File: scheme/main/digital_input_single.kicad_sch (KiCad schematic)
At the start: 5 parts, among them U22 PC817

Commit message: di & do terminals
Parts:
- added D11: BAS40-04, Package_TO_SOT_SMD:SOT-23, symbol Diode:BAS40-04
- renumbered C94 to C96, R75 to R79, R74 to R80, R78 to R81, U22 to U23
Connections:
- net in-: now also D11.1
- net at C96.1, R80.1, R81.2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: now also D11.2, D11.3
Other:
- moved on the sheet: C96, R80, R81

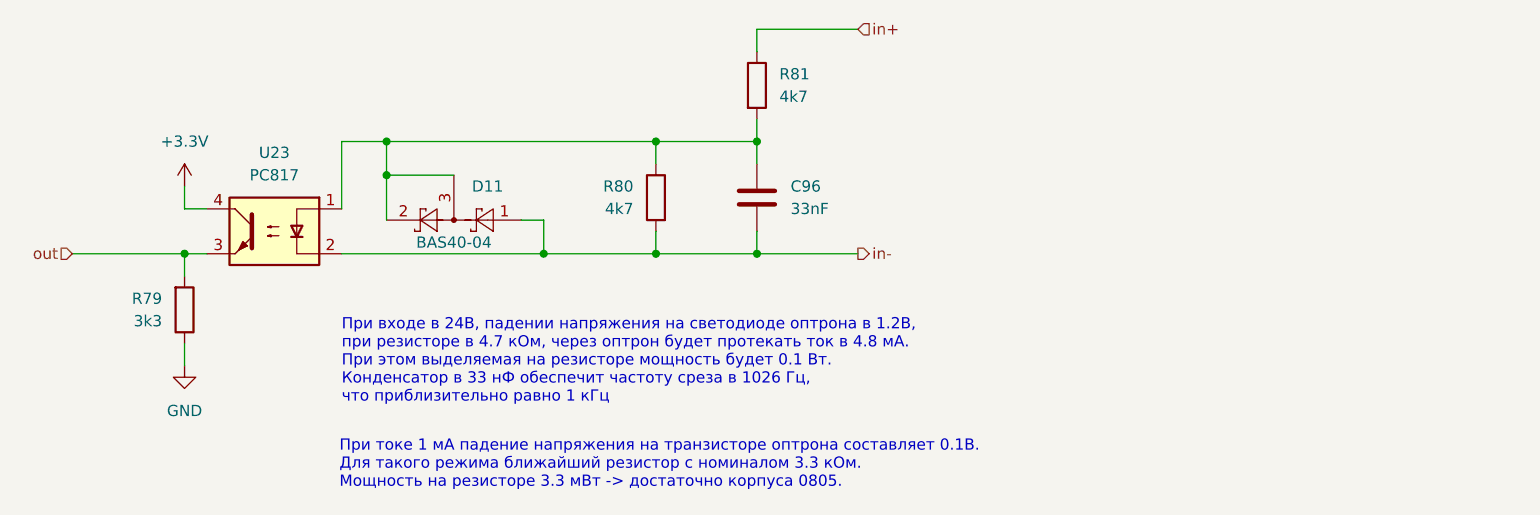
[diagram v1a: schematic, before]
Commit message: dc passive discharge schematic
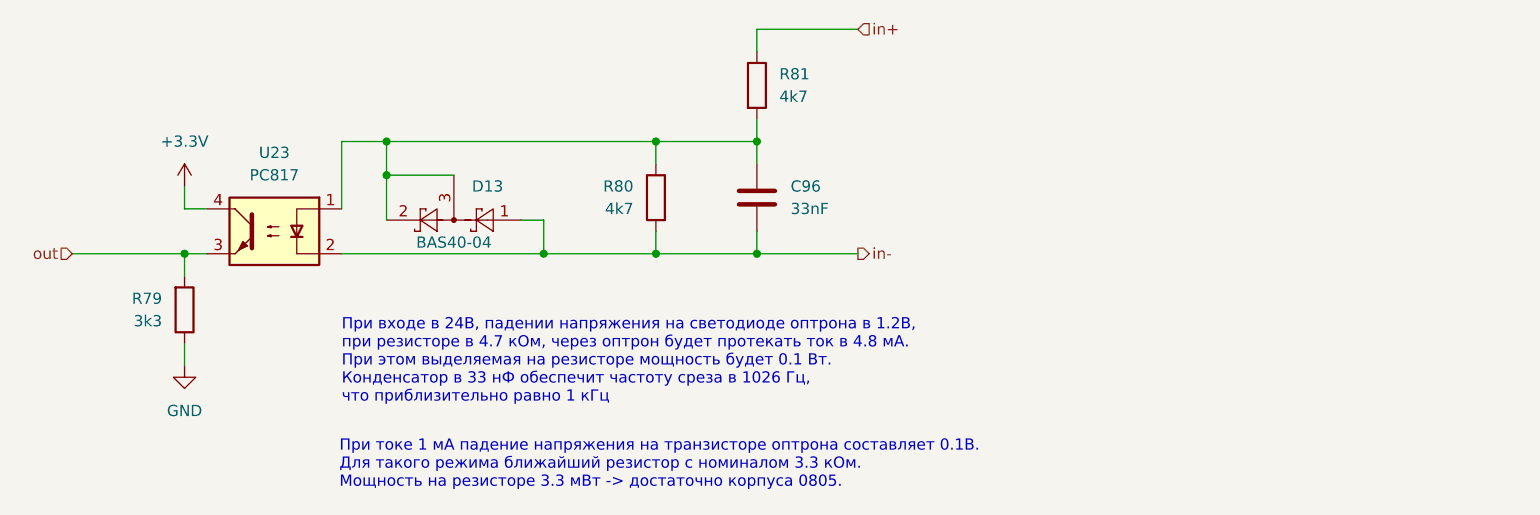
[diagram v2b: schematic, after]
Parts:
- renumbered D11 to D13
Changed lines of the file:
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@@
 		(on_board yes)
 		(dnp no)
-		(property "Reference" "D11"
+		(property "Reference" "D13"
 			(at 161.29 87.63 0)
 			(effects

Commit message: toplevel layout, can bus
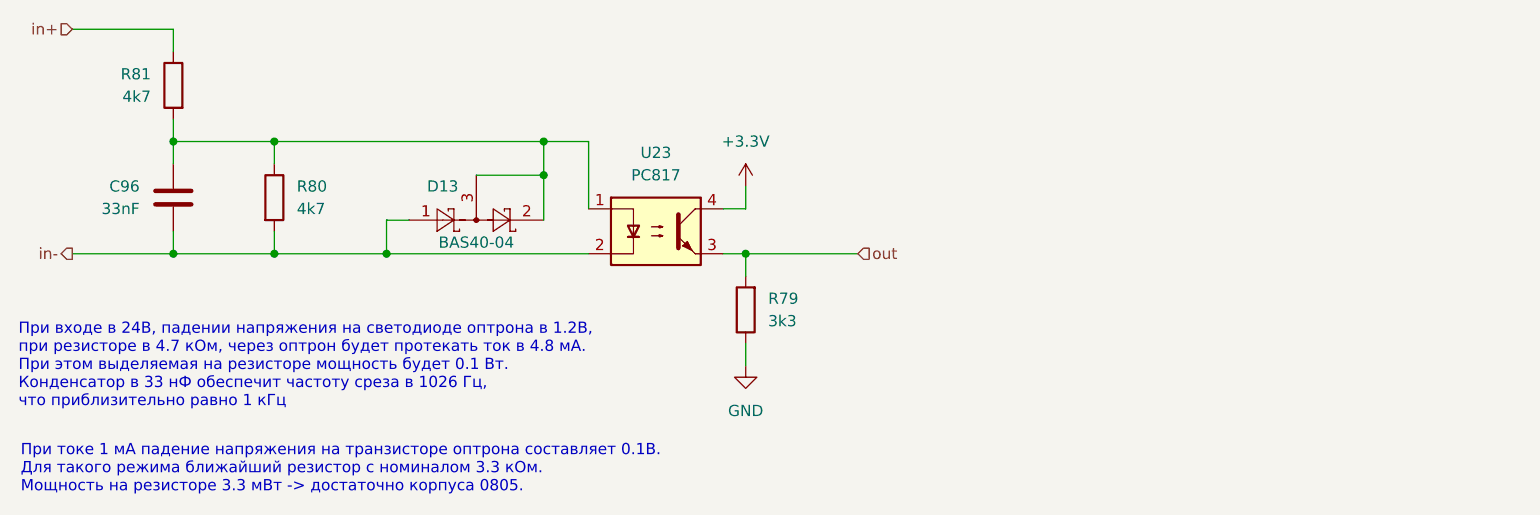
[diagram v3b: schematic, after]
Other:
- moved on the sheet: C96, D13, R79, R80, R81, U23

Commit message: boards schematic sheets & more
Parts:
- added R108: 22R, Resistor_SMD:R_0805_2012Metric, symbol Device:R
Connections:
- net out: now also R108.2; no longer R79.2, U23.3
- new net: R108.1, R79.2, U23.3
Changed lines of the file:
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@@
+	)
+	(junction
+		(at 190.5 95.25)
+		(diameter 0)
+		(color 0 0 0 0)
 	)
 	(junction
@@
 	)
 	(junction
-		(at 190.5 95.25)
-		(diameter 0)
-		(color 0 0 0 0)
-	)
-	(junction
 		(at 125.73 95.25)
 		(diameter 0)
@@
 	(wire
 		(pts
+			(xy 190.5 95.25) (xy 193.04 95.25)
+		)
+		(stroke
+			(width 0)
+			(type default)
+		)
+	)
+	(wire
+		(pts
 			(xy 172.72 95.25) (xy 149.86 95.25)
 		)
@@
 	(wire
 		(pts
-			(xy 203.2 95.25) (xy 190.5 95.25)
-		)
-		(stroke
-			(width 0)
-			(type default)
-		)
-	)
-	(wire
-		(pts
 			(xy 125.73 92.71) (xy 125.73 95.25)
 		)
@@
 		(pts
 			(xy 149.86 95.25) (xy 137.16 95.25)
+		)
+		(stroke
+			(width 0)
+			(type default)
+		)
+	)
+	(wire
+		(pts
+			(xy 200.66 95.25) (xy 203.2 95.25)
 		)
 		(stroke
@@
 					(unit 1)
 				)
+			)
+		)
+	)
+	(symbol
+		(lib_id "Device:R")
+		(at 196.85 95.25 90)
+		(unit 1)
+		(exclude_from_sim no)
+		(in_bom yes)
+		(on_board yes)
+		(dnp no)
+		(fields_autoplaced yes)
+		(property "Reference" "R108"
+			(at 196.85 88.9 90)
+			(effects
+				(font
+					(size 1.27 1.27)
+				)
+			)
+		)
+		(property "Value" "22R"
+			(at 196.85 91.44 90)
+			(effects
+				(font
+					(size 1.27 1.27)
+				)
+			)
+		)
+		(property "Footprint" "Resistor_SMD:R_0805_2012Metric"
+			(at 196.85 97.028 90)
+			(effects
+				(font
+					(size 1.27 1.27)
+				)
+				(hide yes)
+			)
+		)
+		(property "Datasheet" "~"
+			(at 196.85 95.25 0)
+			(effects
+				(font
+					(size 1.27 1.27)
+				)
+				(hide yes)
+			)
+		)
+		(property "Description" "Resistor"
+			(at 196.85 95.25 0)
+			(effects
+				(font
+					(size 1.27 1.27)
+				)
+				(hide yes)
+			)
+		)
+		(pin "1"
+		)
+		(pin "2"
+		)
+		(instances
+			(project "main"
+				(path "/c11d1dbc-4db9-4712-8d1d-5f6f7086cded/bedea6de-a196-4917-ba70-c071156ad9b9/31162724-615b-46ba-8c0e-f604e9ec35b9"
+					(reference "R110")
+					(unit 1)
+				)
+				(path "/c11d1dbc-4db9-4712-8d1d-5f6f7086cded/bedea6de-a196-4917-ba70-c071156ad9b9/9dc33930-f682-4ed1-a57d-b39bd6b7930d"
+					(reference "R109")
+					(unit 1)
+				)
+				(path "/c11d1dbc-4db9-4712-8d1d-5f6f7086cded/bedea6de-a196-4917-ba70-c071156ad9b9/a9420b45-d901-4429-a945-3bcdca919a43"
+					(reference "R108")
+					(unit 1)
+				)
+				(path "/c11d1dbc-4db9-4712-8d1d-5f6f7086cded/bedea6de-a196-4917-ba70-c071156ad9b9/bd001503-3ad8-4979-953f-3e7ea894eb19"
+					(reference "R111")
+					(unit 1)
+				)

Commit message: sort some sheets
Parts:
- renumbered R108 to R110
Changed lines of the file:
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@@
 		(dnp no)
 		(fields_autoplaced yes)
-		(property "Reference" "R108"
+		(property "Reference" "R110"
 			(at 196.85 88.9 90)
 			(effects
